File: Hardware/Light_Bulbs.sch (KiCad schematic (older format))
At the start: 39 parts, among them J1 DNP, J2 USB_B_Micro, Q1 BC548, U1 PIC18F23K22

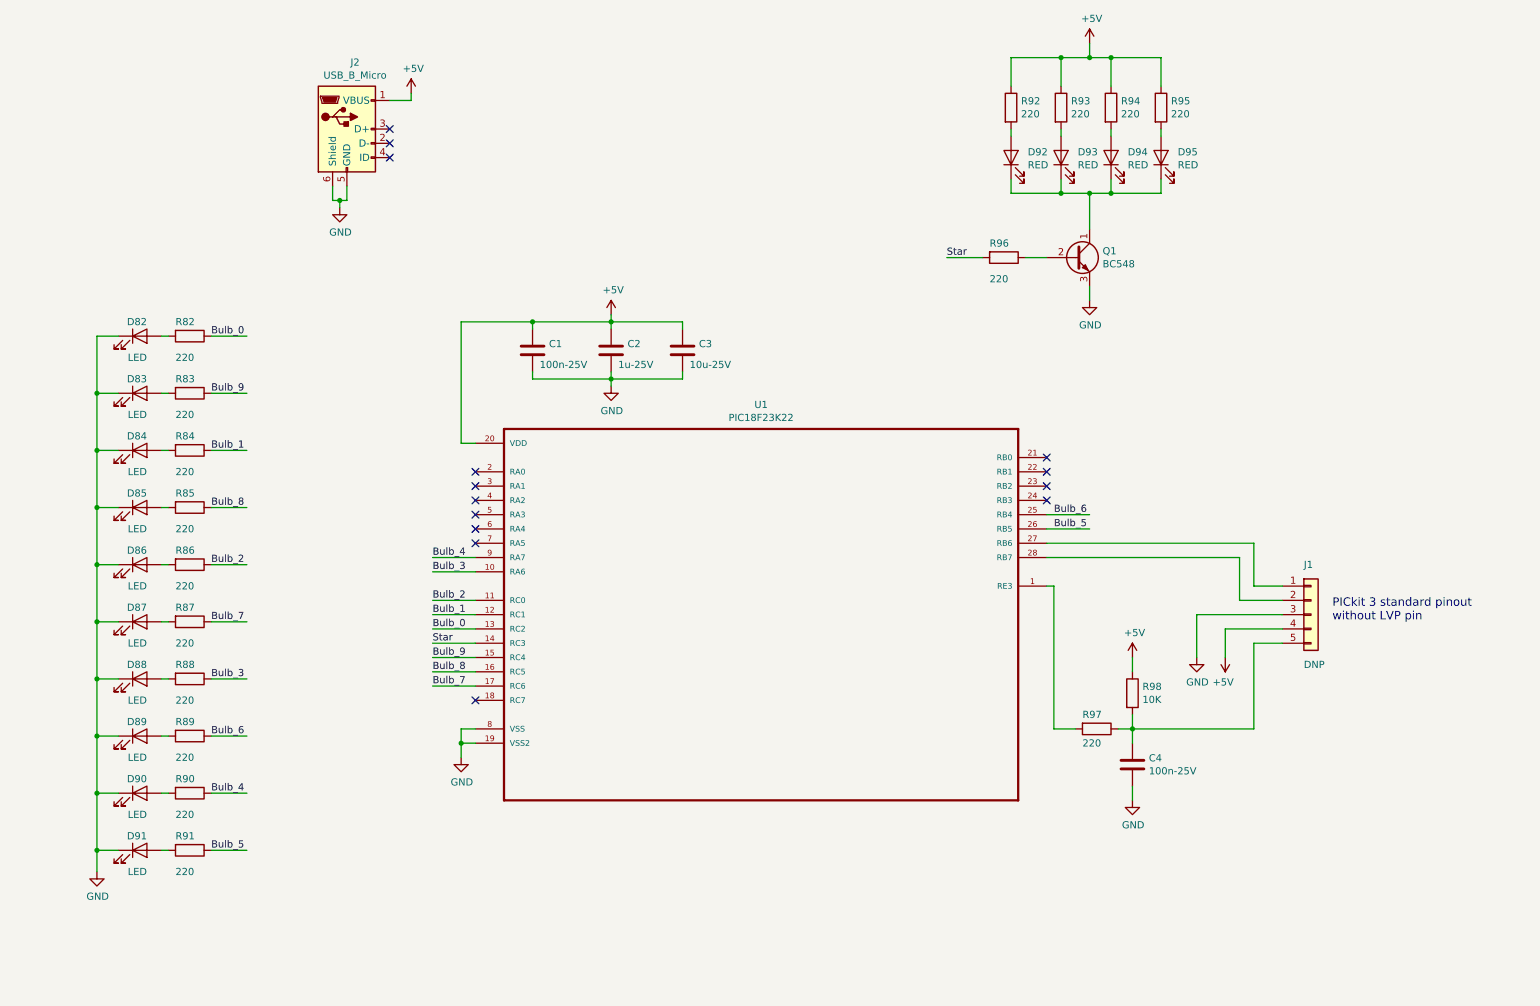
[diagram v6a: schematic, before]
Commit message: Updated schematic and PCB to use microcontroller hardware PWMs to control fairy lights by color and star instead of all light bulbs separately.
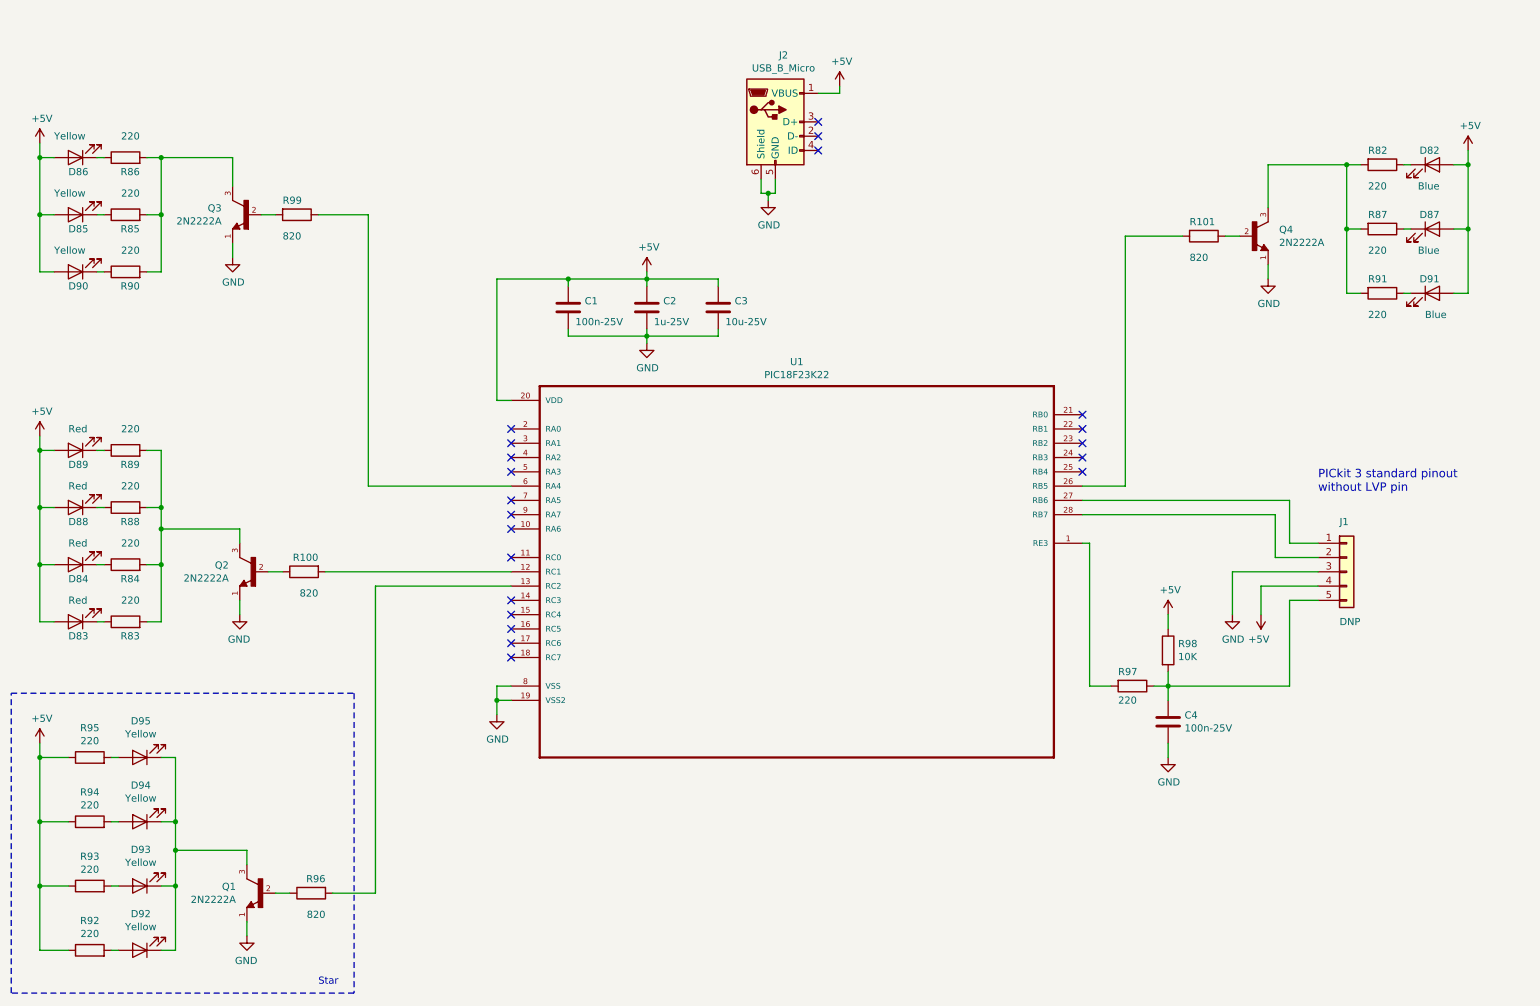
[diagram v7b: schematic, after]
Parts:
- removed Q1: BC548, Package_TO_SOT_THT:TO-92_Inline, symbol Transistor_BJT:BC548
- added Q1, Q2, Q3, Q4: 2N2222A, Package_TO_SOT_THT:TO-18-3, symbol 2N2222A:2N2222A
- added R100, R101, R99: 820, Resistor_THT:R_Axial_DIN0207_L6.3mm_D2.5mm_P7.62mm_Horizontal, symbol Device:R
- D82, D87, D91: value LED -> Blue
- D83, D84, D88, D89: value LED -> Red
- D85, D86, D90: value LED -> Yellow
- D92, D93, D94, D95: value RED -> Yellow
- R96: value 220 -> 820
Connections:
- net labels removed: Bulb_0, Bulb_1, Bulb_2, Bulb_3, Bulb_4, Bulb_5, Bulb_6, Bulb_7, Bulb_8, Bulb_9, Star
- wire segments 123 -> 141
- no-connect marks 14 -> 21
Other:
- note added: "Star"
- moved on the sheet: C1, C2, C3, C4, D82, D83, D84, D85, D86, D87, D88, D89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

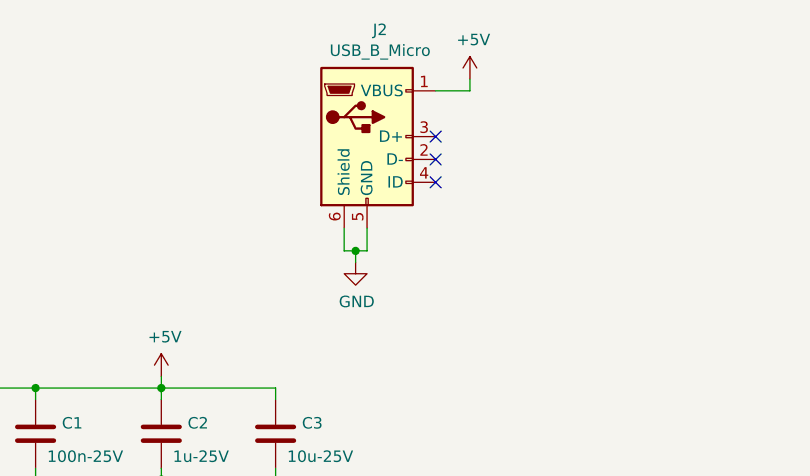
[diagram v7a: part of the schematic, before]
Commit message: Replaced USB micro B connector by a more robust USB B one.
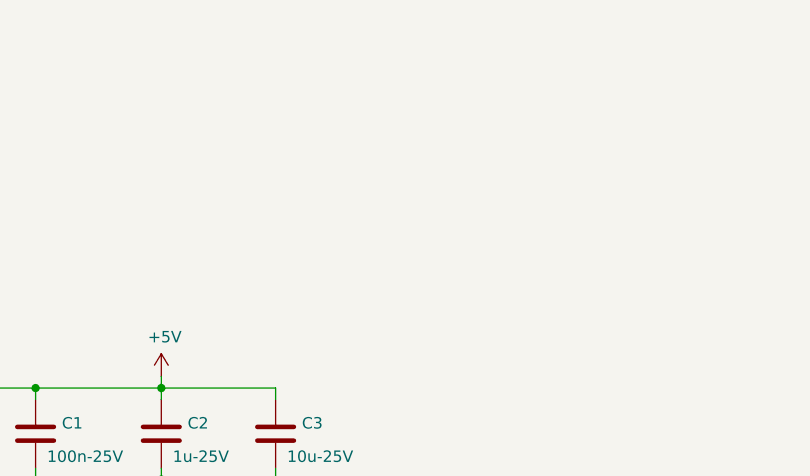
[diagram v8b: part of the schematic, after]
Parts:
- removed J2: USB_B_Micro, Connector_USB:USB_Micro-B_Molex-105017-0001, symbol Connector:USB_B_Micro
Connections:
- no-connect marks 21 -> 18
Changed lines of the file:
@@
 NoConn ~ 4150 5150
-$Comp
-L Connector:USB_B_Micro J2
-U 1 1 60874A52
-P 6000 1400
-F 0 "J2" H 6057 1867 50  0000 C CNN
-F 1 "USB_B_Micro" H 6057 1776 50  0000 C CNN
-F 2 "Connector_USB:USB_Micro-B_Molex-105017-0001" H 6150 1350 50  0001 C CNN
-F 3 "~" H 6150 1350 50  0001 C CNN
-	1    6000 1400
-	1    0    0    -1
-$EndComp
-$Comp
-L power:+5V #PWR0118
-U 1 1 60877195
-P 6450 1150
-F 0 "#PWR0118" H 6450 1000 50  0001 C CNN
-F 1 "+5V" H 6465 1323 50  0000 C CNN
-F 2 "" H 6450 1150 50  0001 C CNN
-F 3 "" H 6450 1150 50  0001 C CNN
-	1    6450 1150
-	1    0    0    -1
-$EndComp
-Wire Wire Line
-	6300 1200 6450 1200
-Wire Wire Line
-	6450 1200 6450 1150
-Wire Wire Line
-	5900 1800 5900 1900
-Wire Wire Line
-	5900 1900 5950 1900
-Wire Wire Line
-	6000 1900 6000 1800
-$Comp
-L power:GND #PWR0119
-U 1 1 6088078F
-P 5950 1950
-F 0 "#PWR0119" H 5950 1700 50  0001 C CNN
-F 1 "GND" H 5955 1777 50  0000 C CNN
-F 2 "" H 5950 1950 50  0001 C CNN
-F 3 "" H 5950 1950 50  0001 C CNN
-	1    5950 1950
-	1    0    0    -1
-$EndComp
-Wire Wire Line
-	5950 1950 5950 1900
-Connection ~ 5950 1900
-Wire Wire Line
-	5950 1900 6000 1900
-NoConn ~ 6300 1400
-NoConn ~ 6300 1500
-NoConn ~ 6300 1600
 $Comp
 L Device:R R?
